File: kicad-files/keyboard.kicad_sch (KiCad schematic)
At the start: 193 parts, among them J1 TYPE-C-31-M12_13, Q1 2N7002, Q2 2N7002, SW1 K2-1187SQ-A4SW-06, T1 53261-0471, T2 53261-0471, U1 STM32F411CEU6, U2 USBLC6-2SC6, U3 AT24C256C-SSHL-T, U4 SGM2007-3.3XN5/TR, Y1 TAXM8M4RFDCET2T

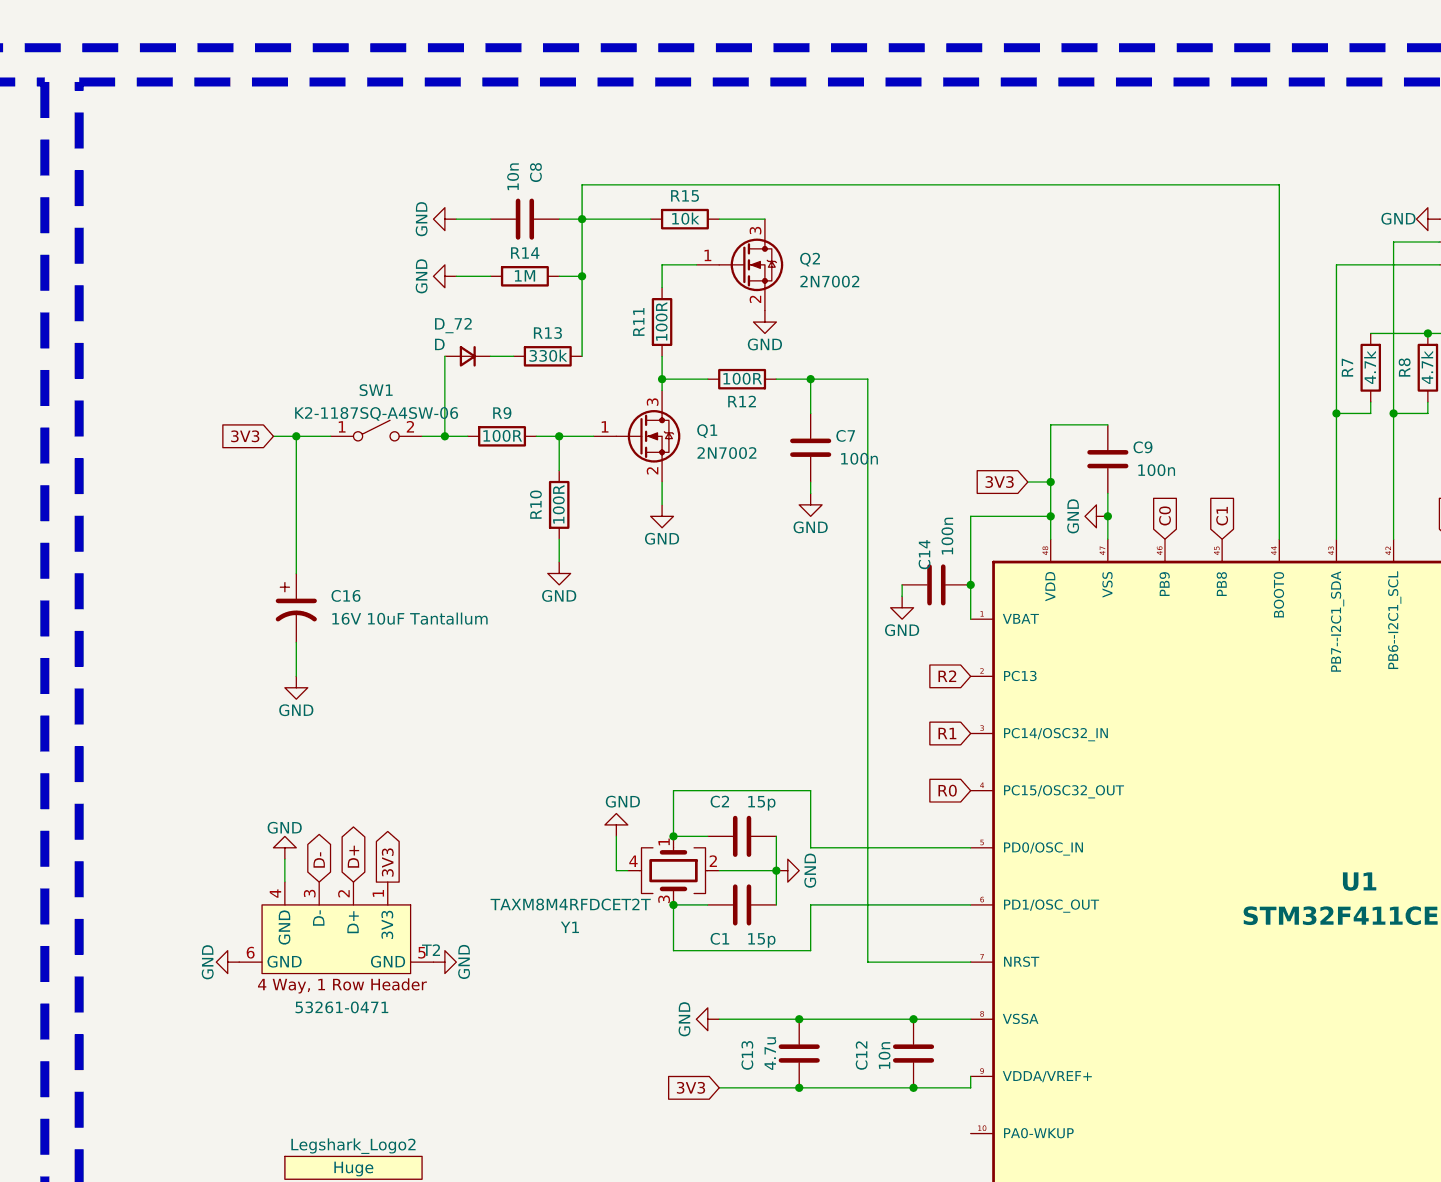
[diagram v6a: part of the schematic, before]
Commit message: Swapped reset switch to less complicated SPDT switch
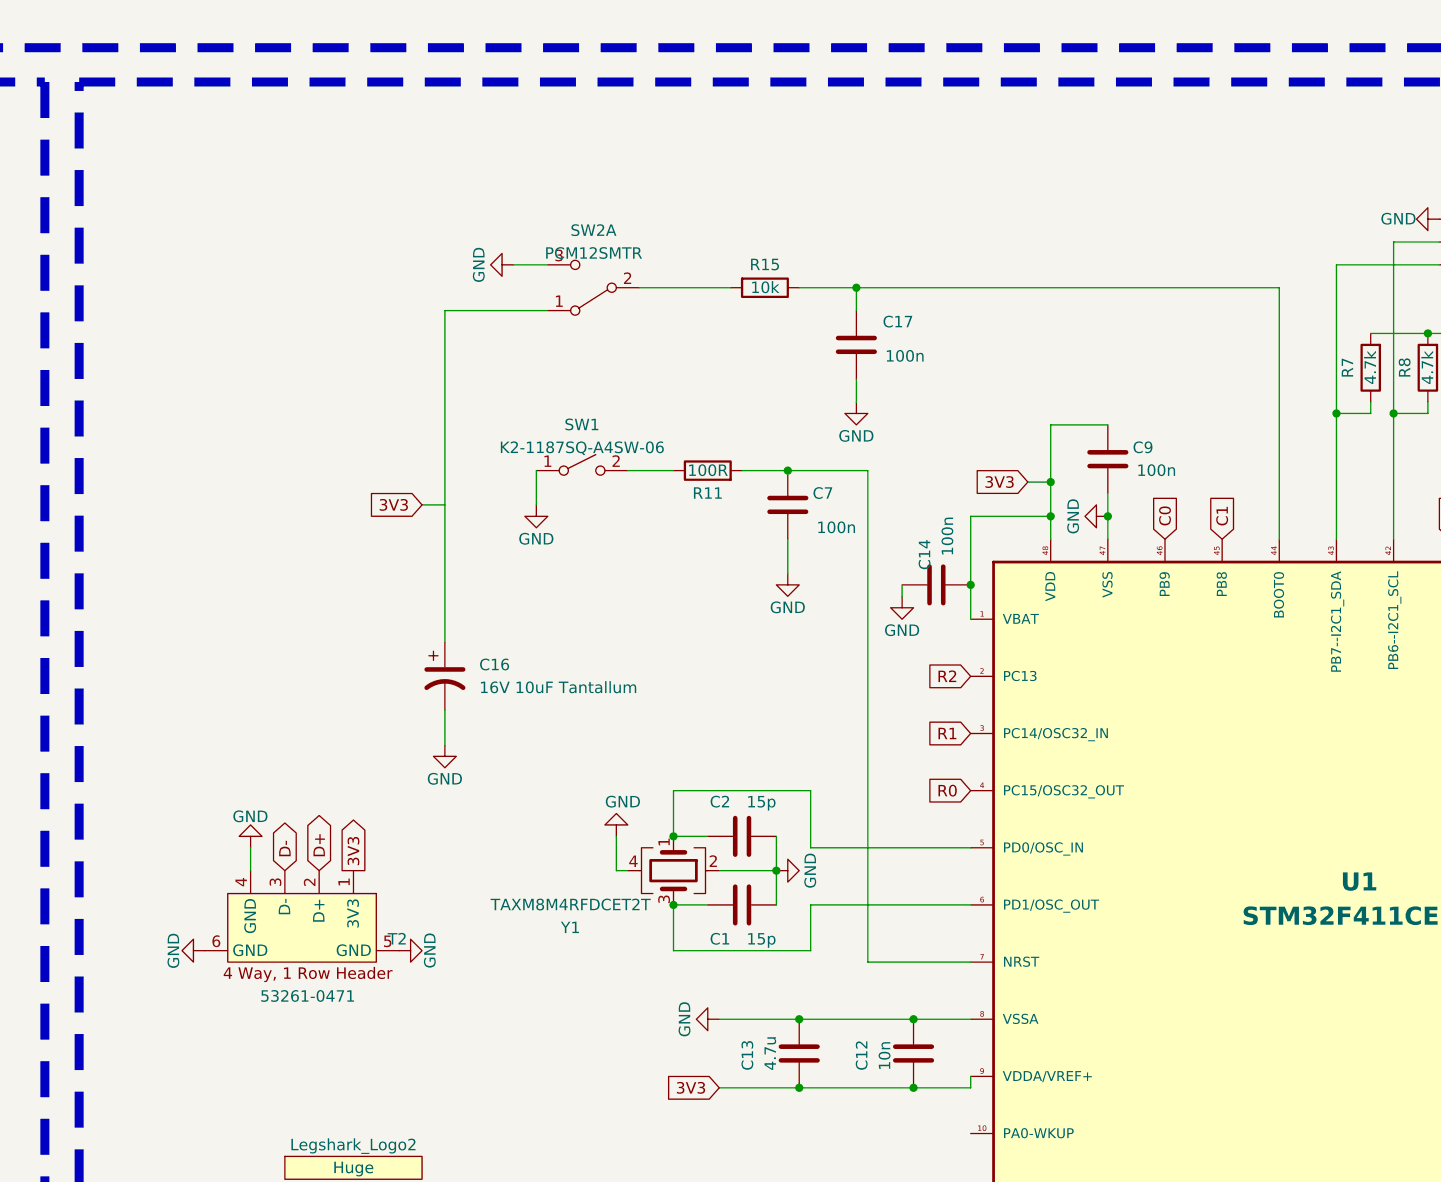
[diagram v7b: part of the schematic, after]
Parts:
- removed C8: 10n, Capacitor_SMD:C_0603_1608Metric_Pad1.08x0.95mm_HandSolder, symbol Device:C
- removed D_72: D, Diode_SMD:D_SOD-123, symbol Device:D_Small
- removed Q1, Q2: 2N7002, Package_TO_SOT_SMD:SOT-23, symbol Transistor_FET:2N7002
- removed R10, R12, R9: 100R, Resistor_SMD:R_0603_1608Metric, symbol Device:R
- removed R13: 330k, Resistor_SMD:R_0603_1608Metric, symbol Device:R
- removed R14: 1M, Resistor_SMD:R_0603_1608Metric, symbol Device:R
- added C17: 100n, Capacitor_SMD:C_0603_1608Metric_Pad1.08x0.95mm_HandSolder, symbol Device:C
- added SW2: PCM12SMTR, Button_Switch_SMD:SW_DPDT_CK_JS202011JCQN, symbol Switch:SW_DPDT_x2
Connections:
- net 3V3: no longer C16.1, SW1.1 (A)
- net GND: now also SW1.1 (A), C17.1, SW2.3 (C)
- net at R15.2: now also SW2.2 (B); no longer U1.44 (BOOT0)
- net at R11.2: now also C7.2, U1.7 (NRST)
- net at R11.1: now also SW1.2 (B)
- net at R15.1: now also U1.44 (BOOT0), C17.2
- new net: C16.1, SW2.1 (A)
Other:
- moved on the sheet: C16, C7, R11, R15, SW1, T2

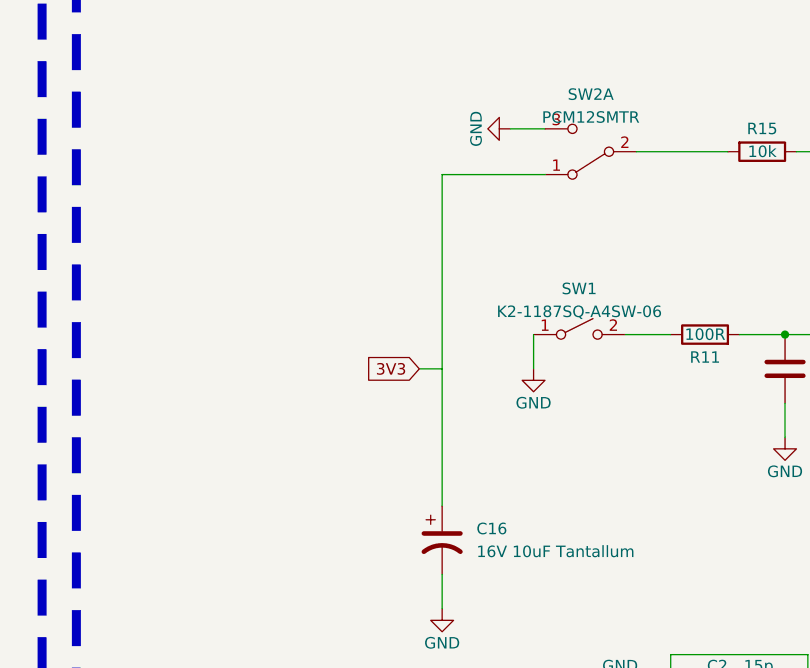
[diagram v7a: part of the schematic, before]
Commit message: Re connected the new reset functionality
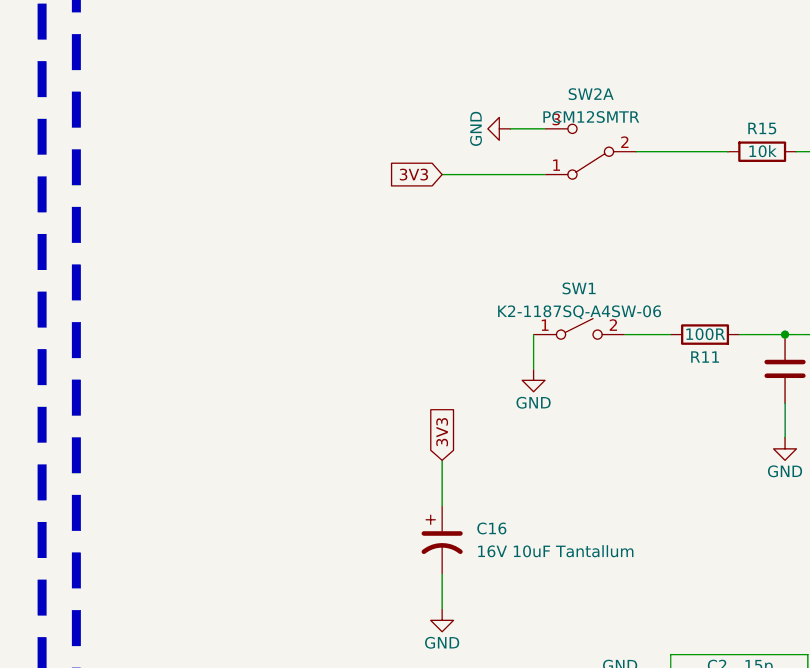
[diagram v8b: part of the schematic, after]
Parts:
- SW2: footprint Button_Switch_SMD:SW_DPDT_CK_JS202011JCQN -> Legshark:Surface Mount Slide Switch SPDT
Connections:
- net 3V3: now also C16.1, SW2.1 (A)
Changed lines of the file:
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@@
-    (stroke (width 0) (type default))
-  )
-  (wire (pts (xy 443.23 339.09) (xy 445.77 339.09))
     (stroke (width 0) (type default))
   )
@@
     (stroke (width 0) (type default))
   )
-  (wire (pts (xy 445.77 317.5) (xy 445.77 354.33))
-    (stroke (width 0) (type default))
-  )
   (wire (pts (xy 604.52 248.92) (xy 604.52 250.19))
     (stroke (width 0) (type default))
@@
   )
   (wire (pts (xy 248.92 223.52) (xy 248.92 224.79))
+    (stroke (width 0) (type default))
+  )
+  (wire (pts (xy 445.77 349.25) (xy 445.77 354.33))
     (stroke (width 0) (type default))
   )
@@
     )
   )
-  (global_label "3V3" (shape input) (at 443.23 339.09 180) (fields_autoplaced)
-    (effects (font (size 1.27 1.27)) (justify right))
-    (property "Intersheetrefs" "${INTERSHEET_REFS}" (at 437.4708 339.09 0)
-      (effects (font (size 1.27 1.27)) (justify right) hide)
+  (global_label "3V3" (shape input) (at 445.77 349.25 90) (fields_autoplaced)
+    (effects (font (size 1.27 1.27)) (justify left))
+    (property "Intersheetrefs" "${INTERSHEET_REFS}" (at 445.77 343.4908 90)
+      (effects (font (size 1.27 1.27)) (justify left) hide)
     )
   )
@@
     )
   )
+  (global_label "3V3" (shape input) (at 445.77 317.5 180) (fields_autoplaced)
+    (effects (font (size 1.27 1.27)) (justify right))
+    (property "Intersheetrefs" "${INTERSHEET_REFS}" (at 440.0108 317.5 0)
+      (effects (font (size 1.27 1.27)) (justify right) hide)
+    )
+  )
   (global_label "C15" (shape input) (at 551.18 430.53 270) (fields_autoplaced)
     (effects (font (size 1.27 1.27)) (justify right))
@@
       (effects (font (size 1.27 1.27)))
     )
-    (property "Footprint" "Button_Switch_SMD:SW_DPDT_CK_JS202011JCQN" (at 462.28 314.96 0)
-      (effects (font (size 1.27 1.27)) hide)
-    )
+    (property "Footprint" "Legshark:Surface Mount Slide Switch SPDT" (at 462.28 314.96 0)
+      (effects (font (size 1.27 1.27)) hide)
+    )
